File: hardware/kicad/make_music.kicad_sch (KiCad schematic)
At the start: 16 parts, among them J1 LEFT / Pico 1-20, J10 C5 / GP26, J11 Semitone up / GP27, J12 Octave up / GP28, J13 Buzzer 1 / PWM / GP13, J14 Buzzer 2 / PWM / GP12, J15 2.54 mm / 16-way TBD, J2 RIGHT / Pico 21-40, J3 C4 / GP16, J4 D4 / GP17, J5 E4 / GP18, J6 F4 / GP19, J7 G4 / GP20, J8 A4 / GP21, J9 B4 / GP22, X1 Logical interface - no footpr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

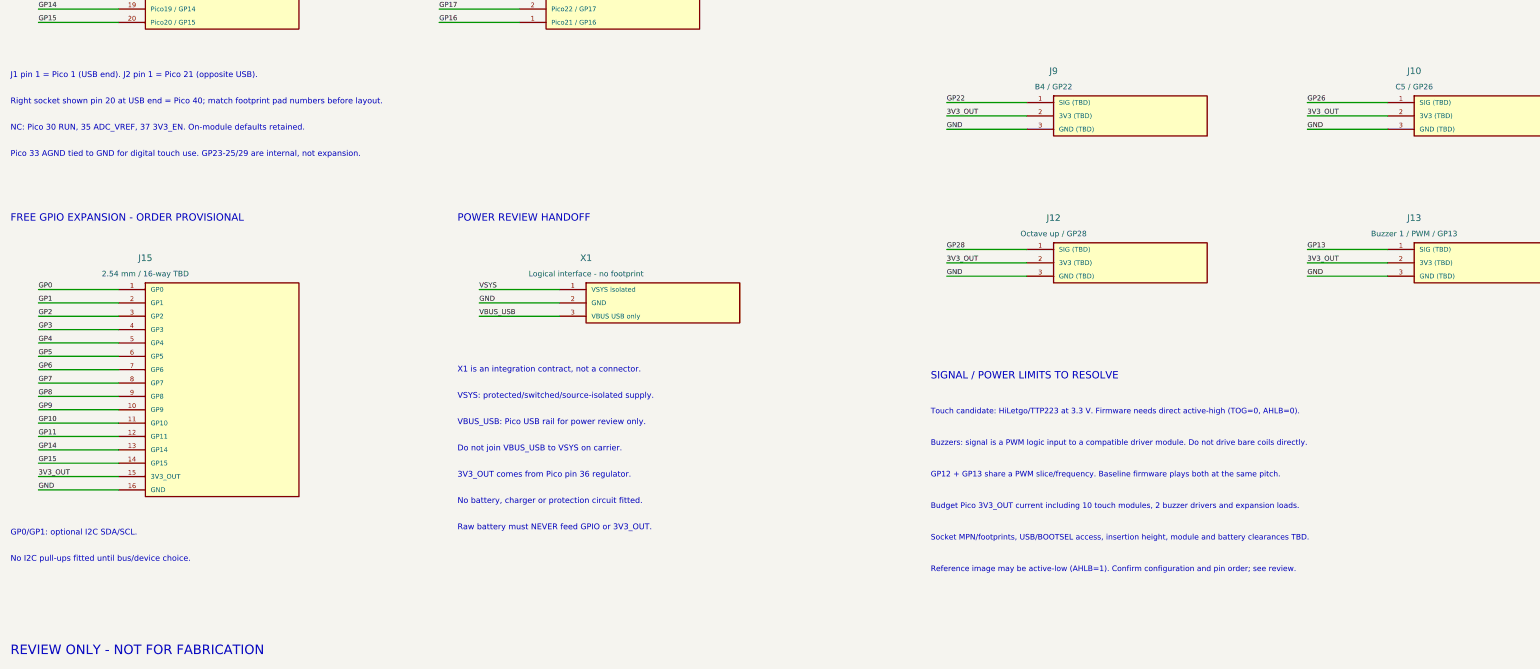
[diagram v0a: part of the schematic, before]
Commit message: Assign candidate Pico socket footprints and document placement orientation
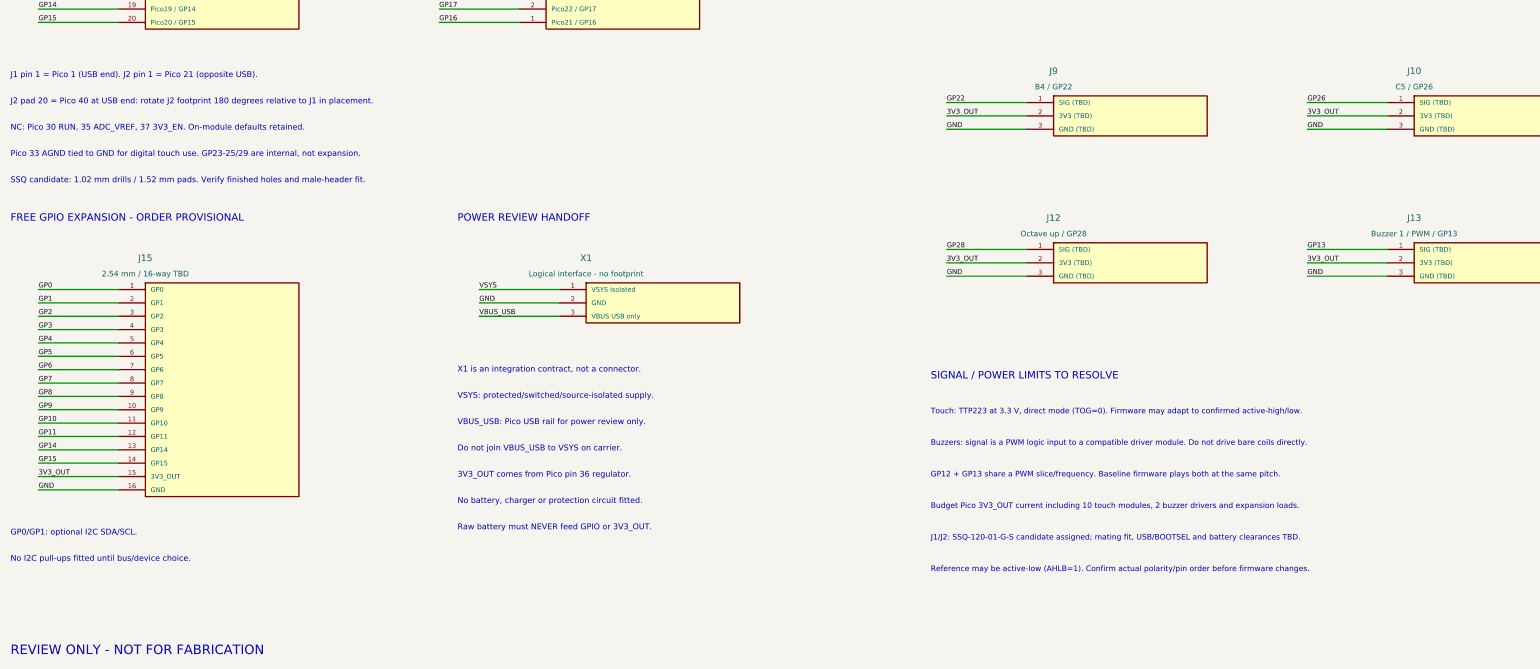
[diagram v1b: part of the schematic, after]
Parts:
- J1, J2: footprint (none) -> MakeMusic:Samtec_SSQ-120-01-G-S_1x20_P2.54mm
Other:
- note added: "J1/J2: SSQ-120-01-G-S candidate assigned; mating fit, USB/BOOTSEL and battery clearances TBD."
- note added: "J2 pad 20 = Pico 40 at USB end: rotate J2 footprint 180 degrees relative to J1 in placement."
- note added: "Reference may be active-low (AHLB=1). Confirm actual polarity/pin order before firmware changes."
- note added: "SSQ candidate: 1.02 mm drills / 1.52 mm pads. Verify finished holes and male-header fit."
- note added: "Touch: TTP223 at 3.3 V, direct mode (TOG=0). Firmware may adapt to confirmed active-high/low."
- note removed: "Reference image may be active-low (AHLB=1). Confirm configuration and pin order; see review."
- note removed: "Right socket shown pin 20 at USB end = Pico 40; match footprint pad numbers before layout."
- note removed: "Socket MPN/footprints, USB/BOOTSEL access, insertion height, module and battery clearances TBD."
- note removed: "Touch candidate: HiLetgo/TTP223 at 3.3 V. Firmware needs direct active-high (TOG=0, AHLB=0)."

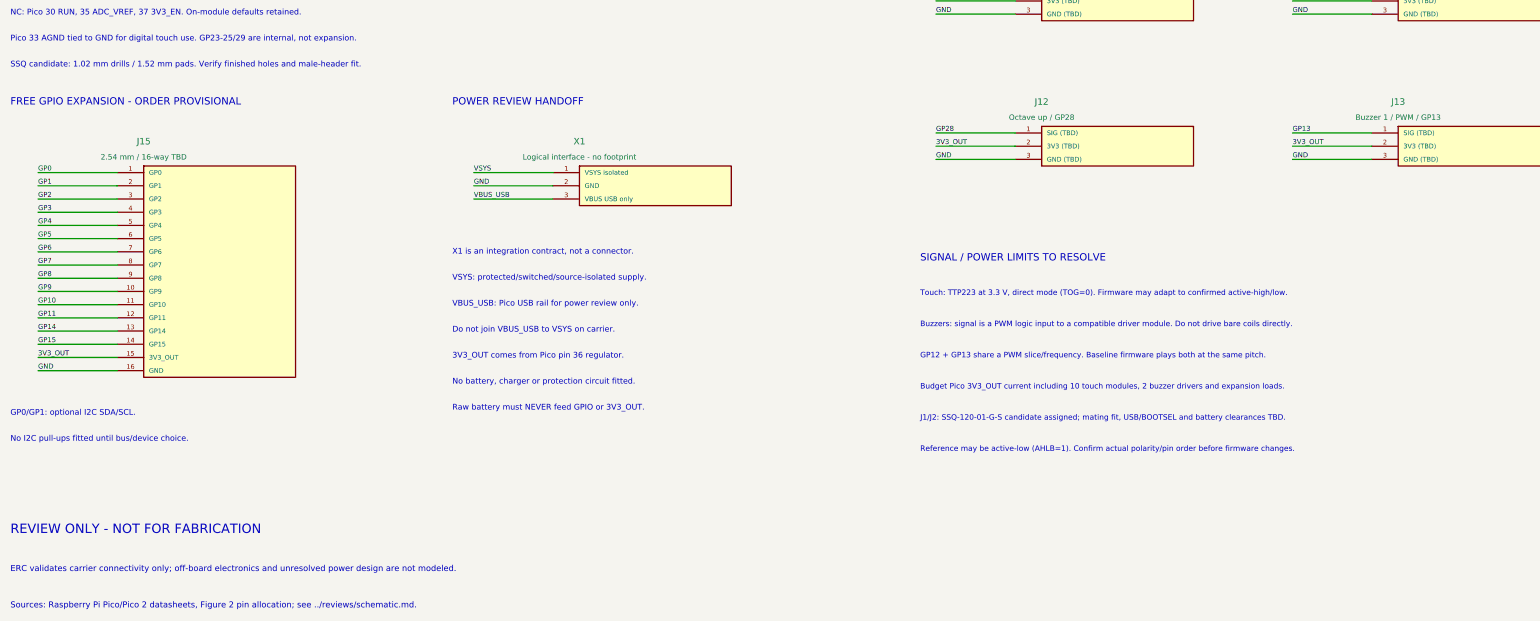
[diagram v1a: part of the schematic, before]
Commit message: Integrate externally charged protected battery switch and isolation circuit
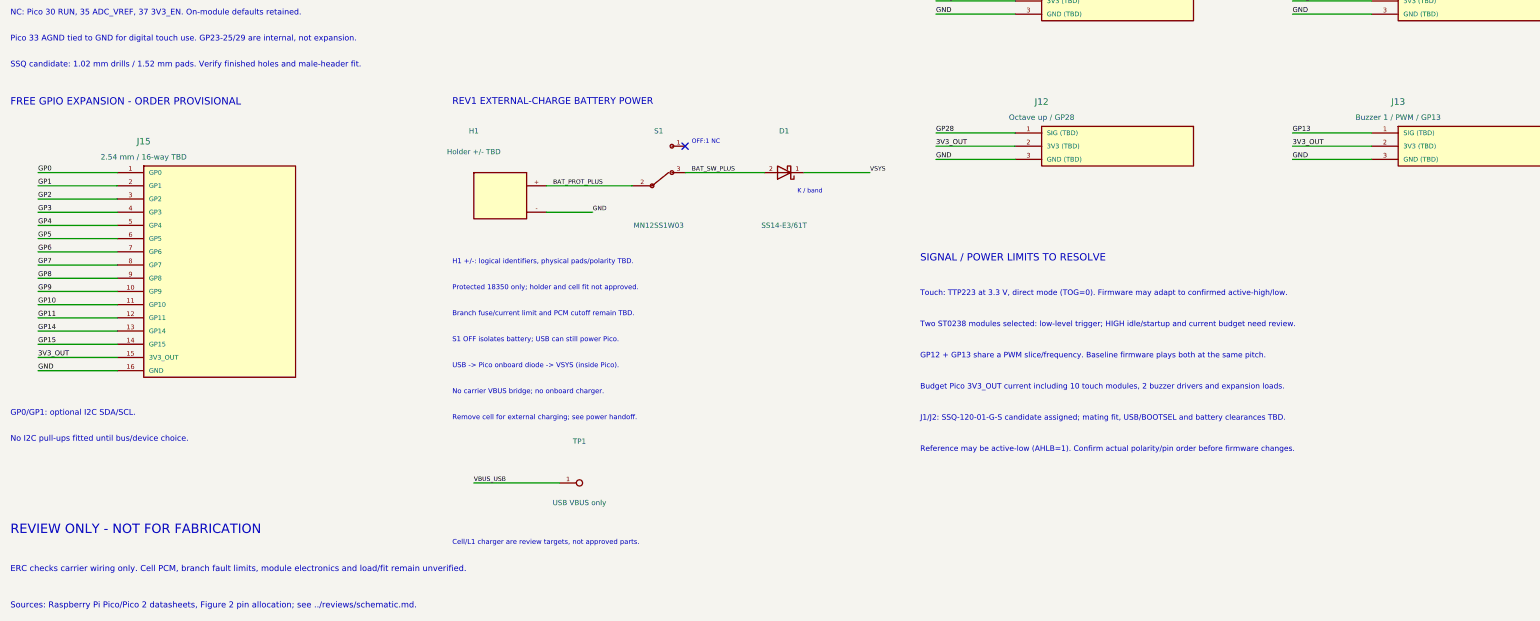
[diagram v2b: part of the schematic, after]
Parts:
- removed X1: Logical interface - no footprint, symbol MakeMusic:Power_Integration
- added D1: SS14-E3/61T, symbol MakeMusic:SS14_K1_A2
- added H1: Holder +/- TBD, symbol MakeMusic:Protected_Cell_Holder_TBD
- added S1: MN12SS1W03, symbol MakeMusic:NKK_MN12_Common2
- added TP1: USB VBUS only, symbol MakeMusic:VBUS_Test_Point
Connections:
- net GND: now also H1.- (PROTECTED_MINUS)
- net VBUS_USB: now also TP1.1 (VBUS)
- net VSYS: now also D1.1 (K)
- new net BAT_PROT_PLUS: H1.+ (PROTECTED_PLUS), S1.2 (COM)
- new net BAT_SW_PLUS: D1.2 (A), S1.3 (BAT_ON)
- no-connect marks 3 -> 4
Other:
- note added: "Branch fuse/current limit and PCM cutoff remain TBD."
- note added: "Cell/L1 charger are review targets, not approved parts."
- note added: "ERC checks carrier wiring only. Cell PCM, branch fault limits, module electronics and load/fit remain unverified."
- note added: "H1 +/-: logical identifiers, physical pads/polarity TBD."
- note added: "K / band"
- note added: "No carrier VBUS bridge; no onboard charger."
- note added: "OFF:1 NC"
- note added: "Protected 18350 only; holder and cell fit not approved."
- note added: "REV1 EXTERNAL-CHARGE BATTERY POWER"
- note added: "Remove cell for external charging; see power handoff."
- note added: "S1 OFF isolates battery; USB can still power Pico."
- note added: "Two ST0238 modules selected: low-level trigger; HIGH idle/startup and current budget need review."
- note added: "USB -> Pico onboard diode -> VSYS (inside Pico)."
- note removed: "3V3_OUT comes from Pico pin 36 regulator."
- note removed: "Buzzers: signal is a PWM logic input to a compatible driver module. Do not drive bare coils directly."
- note removed: "Do not join VBUS_USB to VSYS on carrier."
- note removed: "ERC validates carrier connectivity only; off-board electronics and unresolved power design are not modeled."
- note removed: "No battery, charger or protection circuit fitted."
- note removed: "POWER REVIEW HANDOFF"
- note removed: "Raw battery must NEVER feed GPIO or 3V3_OUT."
- note removed: "VBUS_USB: Pico USB rail for power review only."
- note removed: "VSYS: protected/switched/source-isolated supply."
- note removed: "X1 is an integration contract, not a connector."

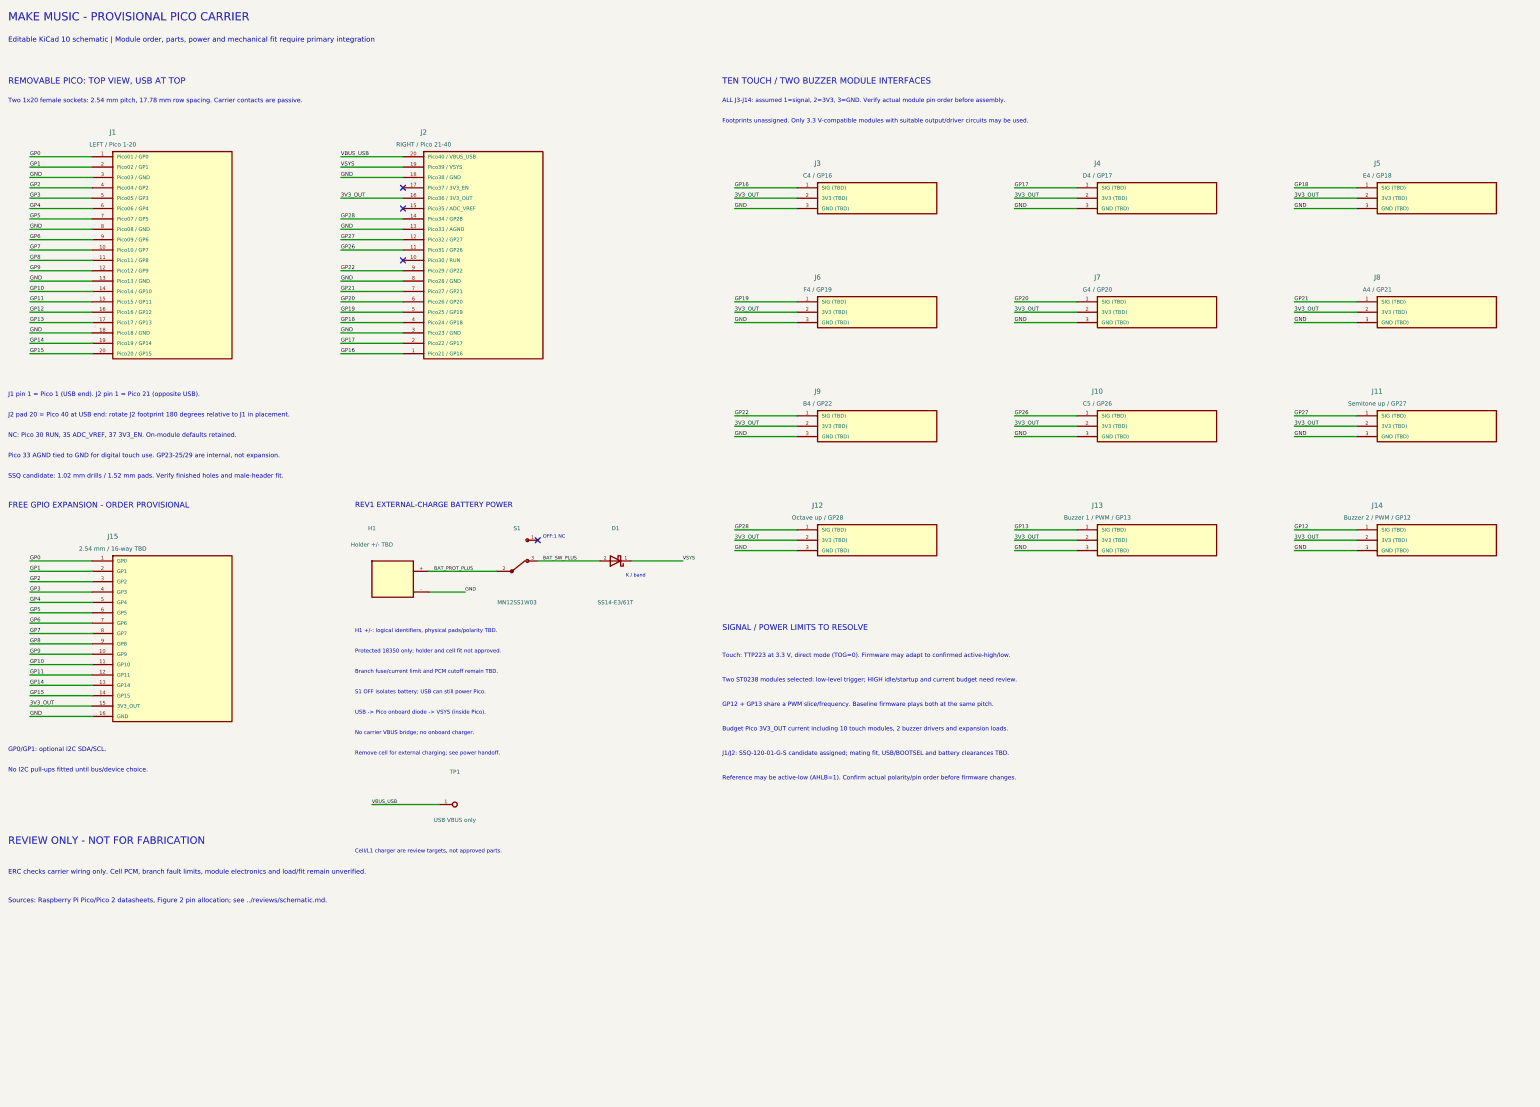
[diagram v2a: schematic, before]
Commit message: Define carrier cable headers, battery harness and buzzer reset bias
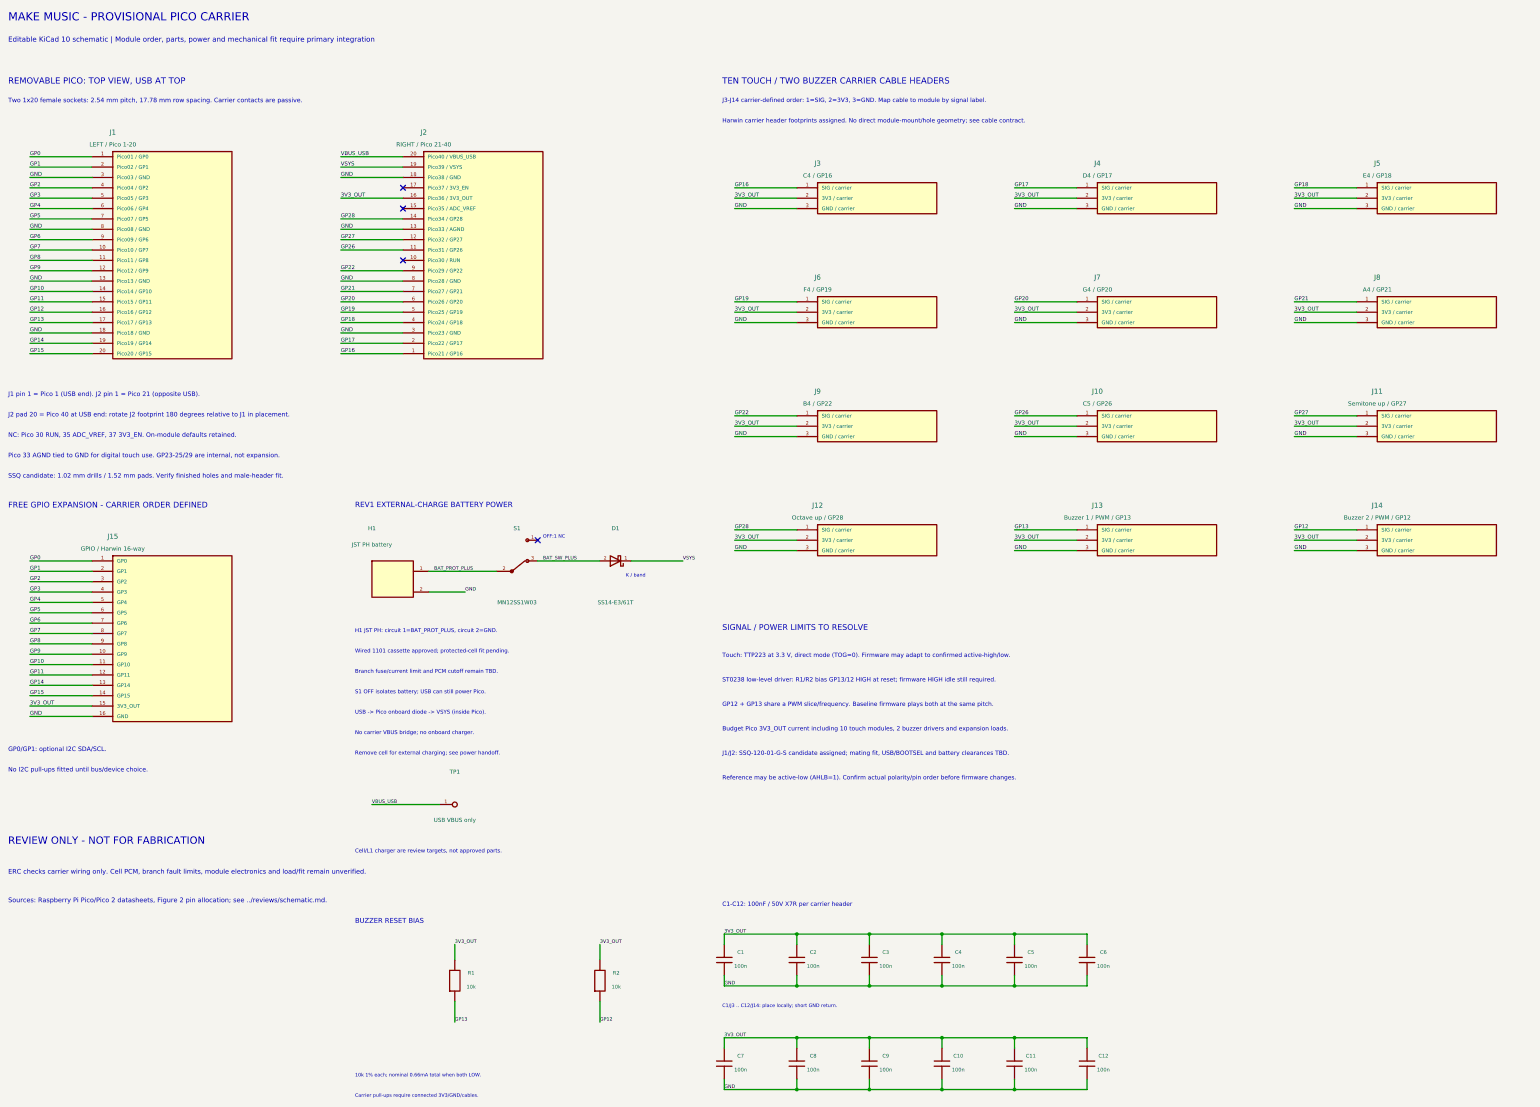
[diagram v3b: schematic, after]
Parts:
- added C1, C10, C11, C12, C2, C3, C4, C5, C6, C7, C8, C9: 100n, MakeMusicCarrier:KEMET_C0603_1608_LevelB, symbol MakeMusic:Carrier_Bypass_Capacitor
- added R1, R2: 10k, Resistor_SMD:R_0603_1608Metric, symbol MakeMusic:Bias_Resistor
- D1: footprint (none) -> MakeMusicCarrier:Vishay_SS14_SMA_K1_A2
- H1: value Holder +/- TBD -> JST PH battery; footprint (none) -> Connector_JST:JST_PH_B2B-PH-K_1x02_P2.00mm_Vertical; symbol MakeMusic:Protected_Cell_Holder_TBD -> MakeMusic:JST_PH_Battery_Harness; MPN (none) -> B2B-PH-K-S(LF)(SN)
- J10, J11, J12, J13, J14, J3, J4, J5, J6, J7, J8, J9: footprint (none) -> MakeMusicCarrier:Harwin_M20-9990346_1x3_P2.54mm; symbol MakeMusic:Module_Interface_3 -> MakeMusic:Carrier_Cable_Header_3; MPN (none) -> M20-9990346
- J15: value 2.54 mm / 16-way TBD -> GPIO / Harwin 16-way; footprint (none) -> MakeMusicCarrier:Harwin_M20-9991646_1x16_P2.54mm; MPN (none) -> M20-9991646
- S1: footprint (none) -> MakeMusicCarrier:NKK_MN12SS1W03_TerminalPattern_Candidate
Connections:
- net 3V3_OUT: now also C1.1, C10.1, C11.1, C12.1, C2.1, C3.1, C4.1, C5.1, C6.1, C7.1, C8.1, C9.1, R1.1, R2.1
- net BAT_PROT_PLUS: now also H1.1 (PROTECTED_PLUS); no longer H1.+ (PROTECTED_PLUS)
- net GND: now also H1.2 (PROTECTED_MINUS), C1.2, C10.2, C11.2, C12.2, C2.2, C3.2, C4.2, C5.2, C6.2, C7.2, C8.2, C9.2; no longer H1.- (PROTECTED_MINUS)
- net GP12: now also R2.2
- net GP13: now also R1.2
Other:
- note added: "10k 1% each; nominal 0.66mA total when both LOW."
- note added: "BUZZER RESET BIAS"
- note added: "C1-C12: 100nF / 50V X7R per carrier header"
- note added: "C1/J3 .. C12/J14: place locally; short GND return."
- note added: "Carrier pull-ups require connected 3V3/GND/cables."
- note added: "FREE GPIO EXPANSION - CARRIER ORDER DEFINED"
- note added: "H1 JST PH: circuit 1=BAT_PROT_PLUS, circuit 2=GND."
- note added: "Harwin carrier header footprints assigned. No direct module-mount/hole geometry; see cable contract."
- note added: "J3-J14 carrier-defined order: 1=SIG, 2=3V3, 3=GND. Map cable to module by signal label."
- note added: "ST0238 low-level driver: R1/R2 bias GP13/12 HIGH at reset; firmware HIGH idle still required."
- note added: "TEN TOUCH / TWO BUZZER CARRIER CABLE HEADERS"
- note added: "Wired 1101 cassette approved; protected-cell fit pending."
- note removed: "ALL J3-J14: assumed 1=signal, 2=3V3, 3=GND. Verify actual module pin order before assembly."
- note removed: "FREE GPIO EXPANSION - ORDER PROVISIONAL"
- note removed: "Footprints unassigned. Only 3.3 V-compatible modules with suitable output/driver circuits may be used."
- note removed: "H1 +/-: logical identifiers, physical pads/polarity TBD."
- note removed: "Protected 18350 only; holder and cell fit not approved."
- note removed: "TEN TOUCH / TWO BUZZER MODULE INTERFACES"
- note removed: "Two ST0238 modules selected: low-level trigger; HIGH idle/startup and current budget need review."
